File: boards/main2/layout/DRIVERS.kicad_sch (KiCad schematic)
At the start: 53 parts, among them IC6 STSPIN958TR, IC8 DRV8874PWPR, IC9 DRV8874PWPR, M1 B02B-PASK(LF)(SN), M2 B02B-PASK(LF)(SN), M3 B02B-PASK(LF)(SN)

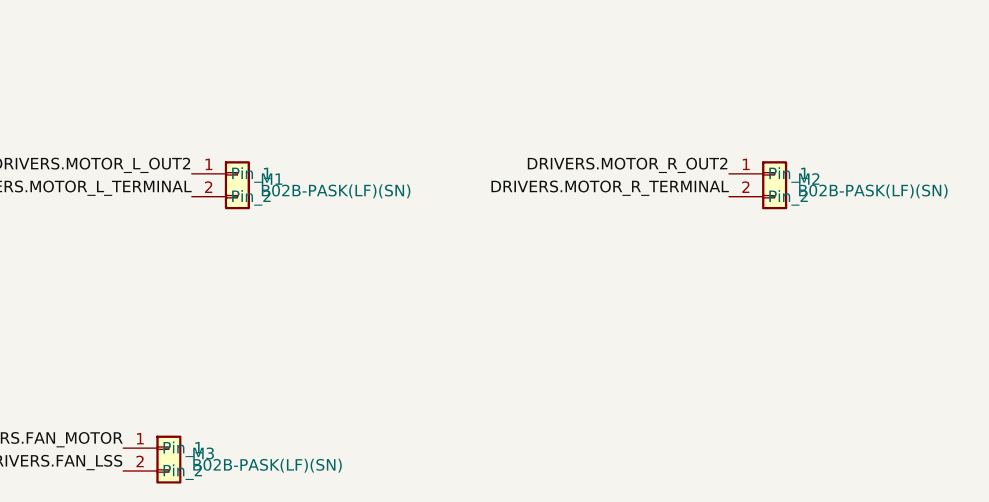
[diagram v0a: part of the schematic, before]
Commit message: 🎨 Place main2's SENSORS sheet, and draw the TLV9001's inputs as + and − in its triangle
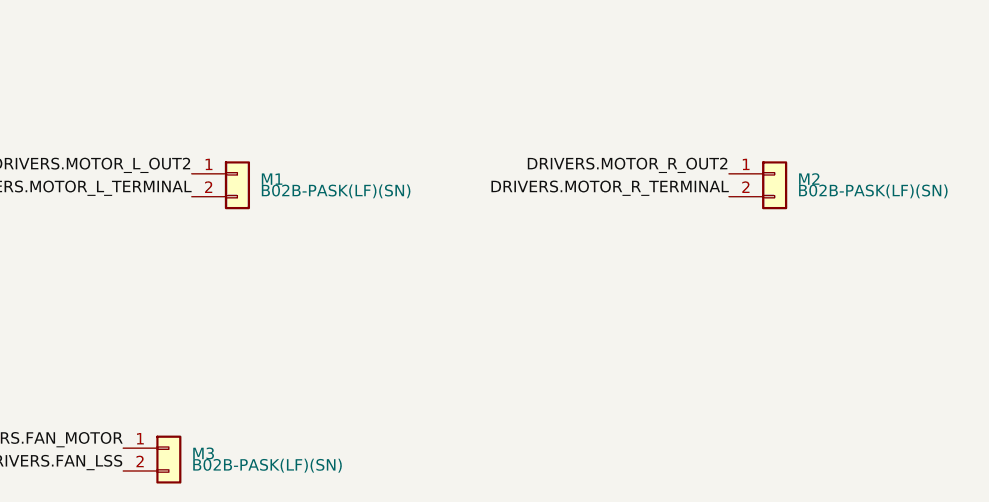
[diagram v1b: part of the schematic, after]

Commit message: 🍱 Regenerate main2's DRIVERS and PERIPHERALS sheets with the widened USBLC6 and the jumper pin labels
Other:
- note added: "Bridge sleep pull-down and fault pull-up (IC8, IC9)"
- note added: "Fan driver: STSPIN958 IC6, one half-bridge, current limit through R31"
- note added: "Left motor (M1): DRV8874 IC9, shunt R75 to the INA241, choke L5"
- note added: "Right motor (M2): DRV8874 IC8, shunt R65 to the INA241, choke L4"
- note added: "Sheet ports"
- title: (none) -> Motor bridges and fan driver
- moved on the sheet: C30, C31, C32, C33, C34, C35, C36, C82, C83, C84, C85, C86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

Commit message: ⚡️ Replace main2's bridge electrolytics with 1210 ceramics, and study VBAT bulk and overvoltage
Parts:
- removed C87, C96: 100uF 20% 25V, Team-Micras_MicrasPCB_components_jierr_JVS25V100M6X4:CAP-SMD_BD6.3-L6.6-W6.6-LS7.3-FD_JVS25V100M6X4, symbol JVS25V100M6X4
- added C111, C112, C87, C96: 10uF 10% 50V X7R, stdlib_kicad-footprints_Capacitor_SMD:C_1210_3225Metric, symbol C_Small
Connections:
- net GND: now also C111.1, C112.1, C87.1, C96.1
- net VBAT: now also C111.2, C112.2, C87.2, C96.2

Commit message: 🚧 Place and route main2 but for 12 connections
place.py places every part and route.py pours the planes and routes the board, with hand-routed
fixes on top. 12 connections are still open (boards/main2/layout/README.md, Layout), so DRC and
the layout check fail on them; every other gate passes.
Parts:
- removed R62, R72: 0, stdlib_kicad-footprints_Resistor_SMD:R_0402_1005Metric, symbol R_Small
- removed R77: 0 1W, stdlib_kicad-footprints_Resistor_SMD:R_2512_6332Metric, symbol R_Small

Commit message: 🐛 Fix main2's review findings and settle its open doubts
Schematic and parts:
- Battery input: F1 is a 12 A Littelfuse 501 (0501012.WR1). C58 now sits
  gate-source with C114 gate-drain, so Q6 stays off at plug-in. D16 clamps
  Q8's VGS. R44/R45 are 10k/2k, so VBAT can't float up on USB alone.
- Capacitors: VBAT and VSYS use 1210/0805 50 V parts, sized with Samsung's
  DC-bias curves. C109 is fitted.
- Drivers: R66/R76 are removed (the chokes are needed). ITRIP and the fan
  limit are retuned. The INA241 R_iso is 150 Ohm.
- Rails are declared as ranges, and the abs-max checks run under the TVS
  clamp.
- STM32 pin swaps for routing: the wall selectors move to TIM3,
  Motor_Left_EN to TIM8_CH2 and LED_ARGB to TIM17. CubeMX 6.18.1 confirms
  the map.
- firmware_changes.toml registers the matching firmware changes: the ADC
  0.7 us sampling time, the TIM4-triggered DAC, the fan's 50 kHz start, a
  wheel-sign self-check, VDDA tracking, contest mode, the debug halt and
  others.

Layout:
- USB D+/D- are routed as a coupled pair. The track floor is 0.12 mm.
- Stubs and detours are trimmed. The In2 VCORE/3V3_D islands are shrunk.
- The board is notched under the ESP32 antenna.
- Ground stitching, thermal reliefs, open thermal vias with split paste,
  DRV8874 heat islands and teardrops are added.
- 11 joins remain for hand-routing (layout README, Open items).

Doubts are closed by datasheets, vendor SPICE models and new research
calculations instead of bench TODOs. Tests cover each review item.
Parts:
- removed C85, C86, C94, C95: 10uF 10% 50V X7R, stdlib_kicad-footprints_Capacitor_SMD:C_1206_3216Metric, symbol C_Small
- removed R66, R76: 0 1W, stdlib_kicad-footprints_Resistor_SMD:R_2512_6332Metric, symbol R_Small
- C33: value 1uF 10% 25V X5R -> 1uF 10% 50V X7R; footprint stdlib_kicad-footprints_Capacitor_SMD:C_0402_1005Metric -> stdlib_kicad-footprints_Capacitor_SMD:C_0805_2012Metric
- C34, C35: footprint stdlib_kicad-footprints_Capacitor_SMD:C_0603_1608Metric -> stdlib_kicad-footprints_Capacitor_SMD:C_0805_2012Metric
- C36, C83, C84, C92, C93, C99: footprint stdlib_kicad-footprints_Capacitor_SMD:C_1206_3216Metric -> stdlib_kicad-footprints_Capacitor_SMD:C_1210_3225Metric
- IC6: footprint Team-Micras_MicrasPCB_components_st_STSPIN958:QFN50P500X500X100-33N-D -> Team-Micras_MicrasPCB_components_st_STSPIN958:QFN50P500X500X100-33N-D_SplitPaste
- R28: value 22k 1% -> 4.7k 1%
- R29: value 9.1k 1% -> 2k 1%
- R63, R73: value 5.6k 1% -> 4.7k 1%
- R64, R74: value 24k 1% -> 20k 1%
